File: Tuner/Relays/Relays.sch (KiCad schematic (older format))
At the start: 82 parts, among them J1 Conn_01x03, J10 Conn_01x02, J11 Conn_01x02, J12 Conn_01x01, J13 Conn_01x01, J14 Conn_01x01, J15 Conn_01x01, J16 Conn_01x02, J17 Conn_02x10_Odd_Even, J18 Conn_01x02, J19 Conn_01x03, J2 Conn_01x03, J3 Conn_01x03, J4 Conn_01x03, J5 Conn_01x03, J6 Conn_01x03, J7 Conn_01x03, J8 Conn_01x02, J9 Conn_01x02

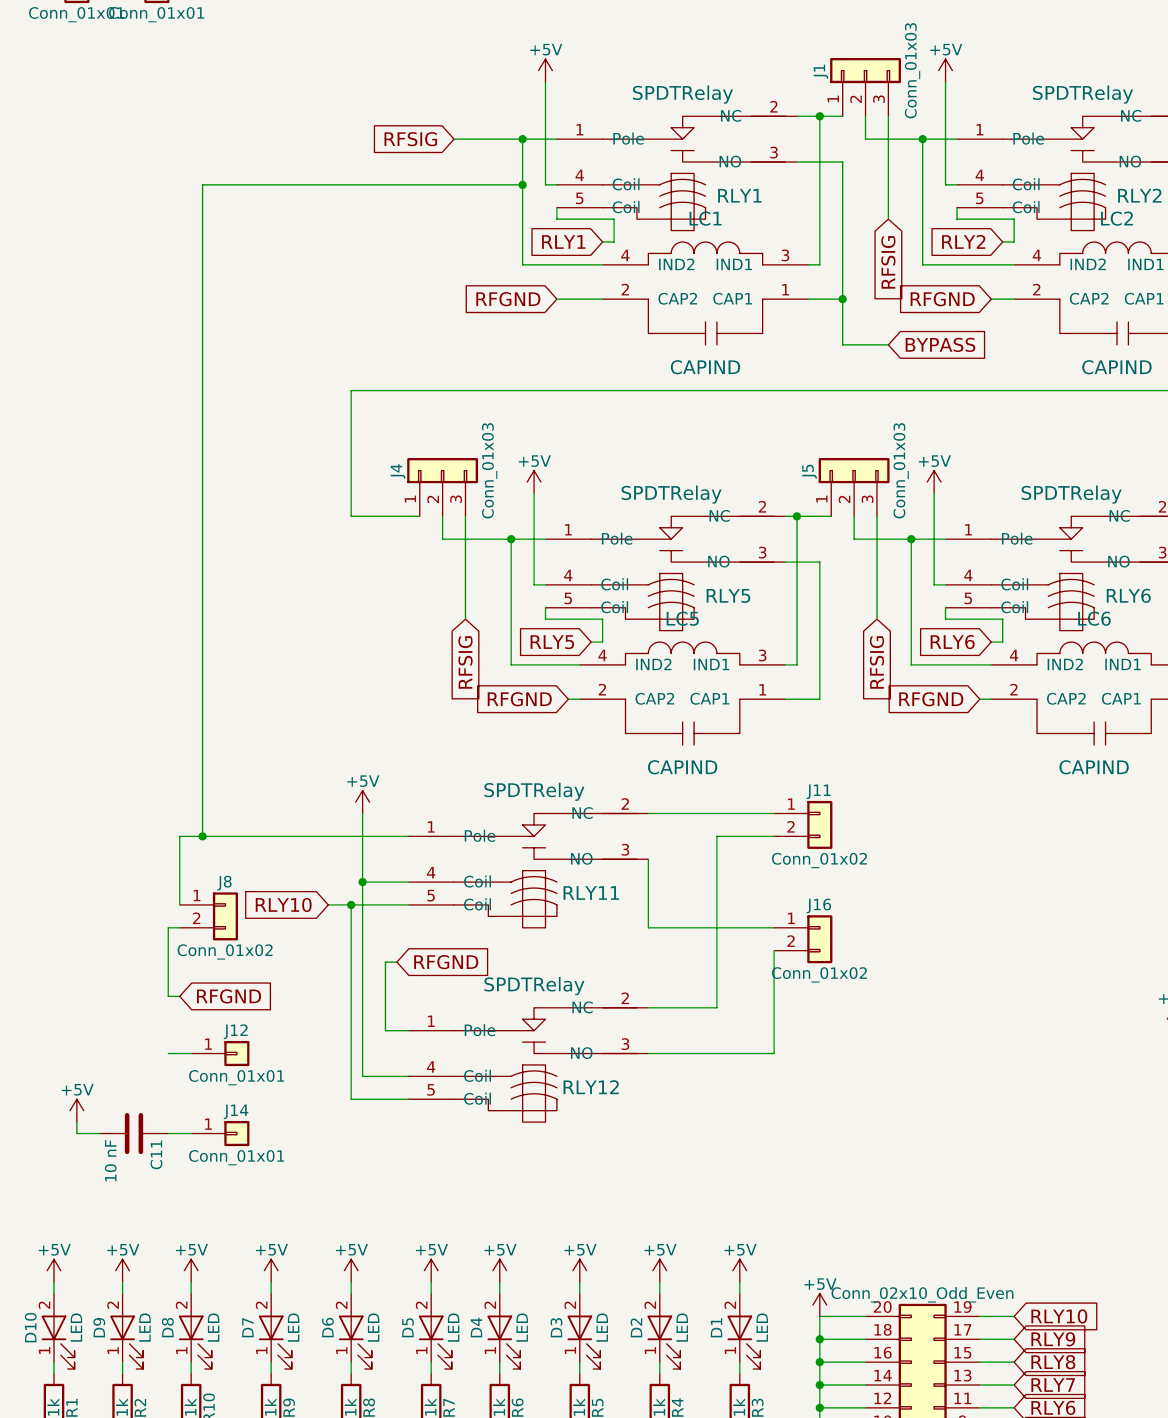
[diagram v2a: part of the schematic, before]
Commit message: Relay boards changed to have coil terminals all on same side
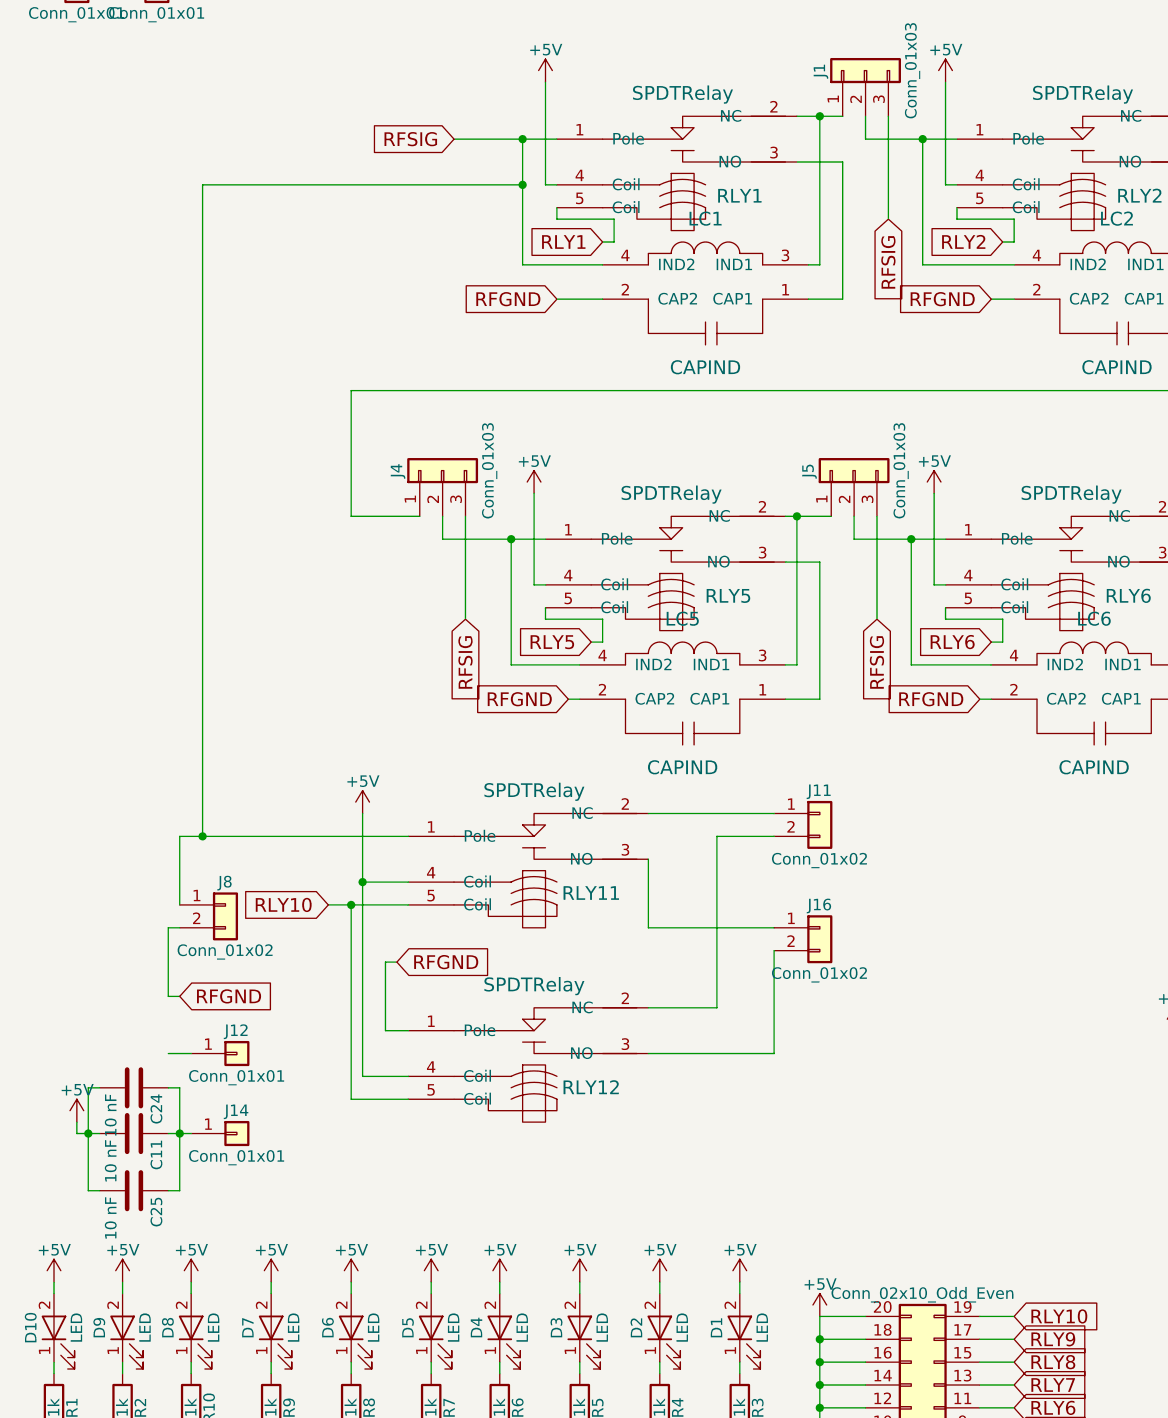
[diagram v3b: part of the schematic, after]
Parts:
- added C24, C25: 10 nF, Capacitors_THT:C_Disc_D5.0mm_W2.5mm_P5.00mm, symbol C
- C11: footprint Capacitors_THT:C_Disc_D5.0mm_W2.5mm_P2.50mm -> Capacitors_THT:C_Disc_D5.0mm_W2.5mm_P5.00mm
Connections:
- net +5V: now also C24.2, C25.2
- net at C11.1, J14.1 (Pin_1): now also C24.1, C25.1
- net BYPASS: no longer names the net of LC1.1 (CAP1), RLY1.3 (NO)

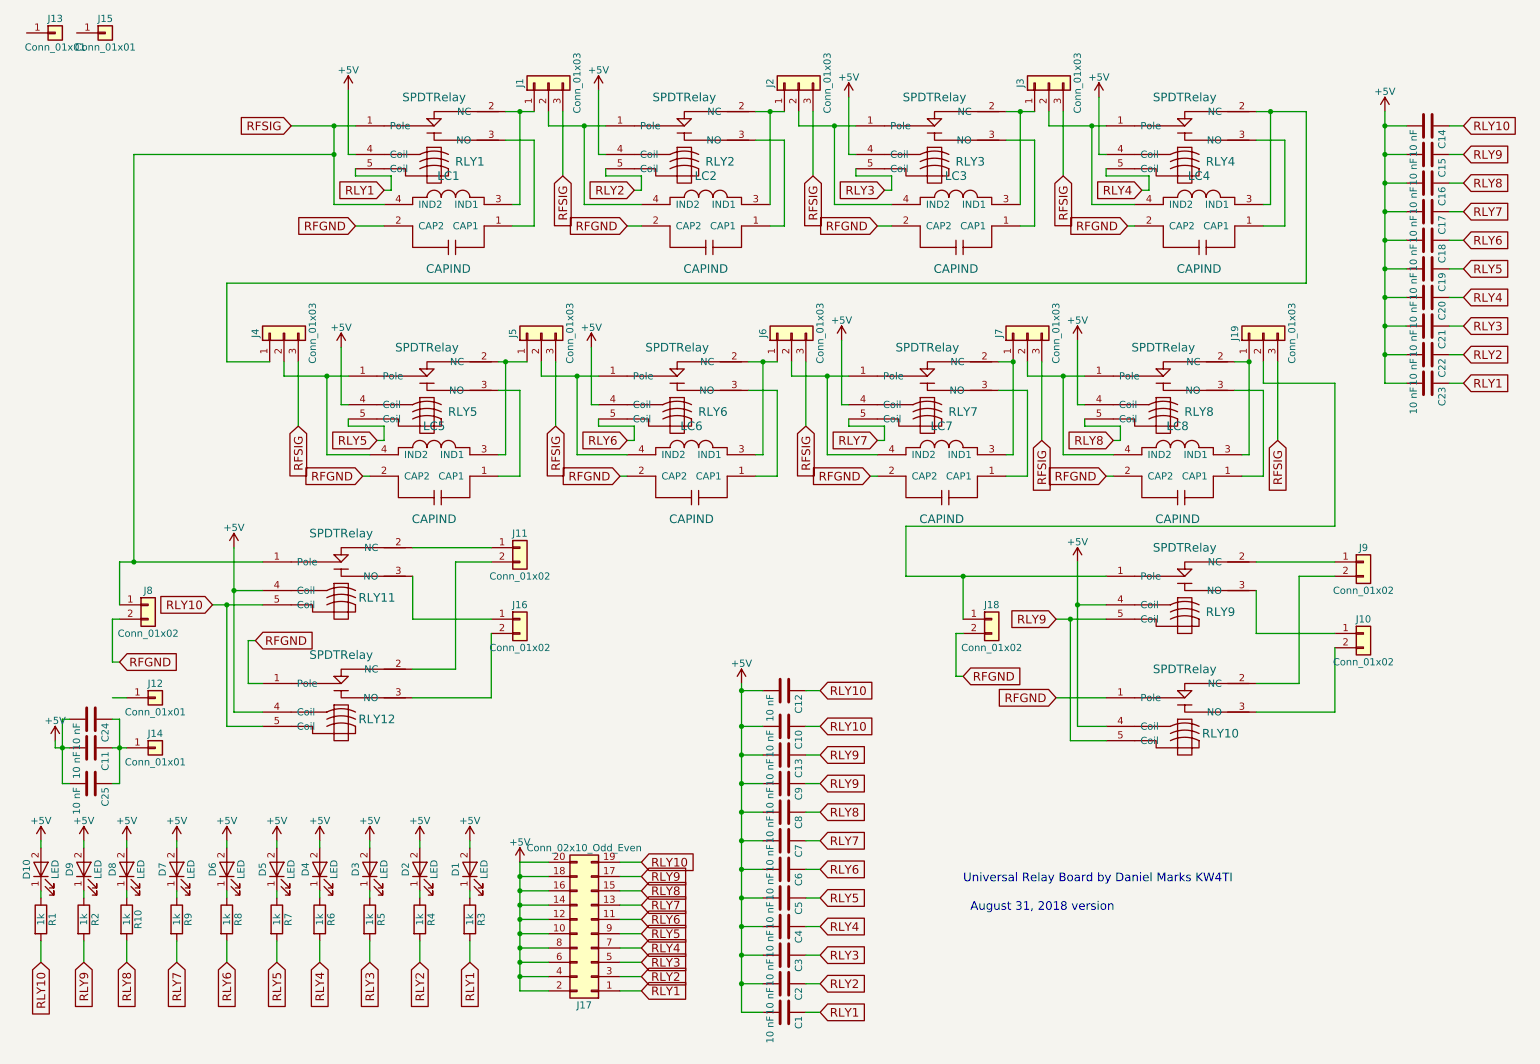
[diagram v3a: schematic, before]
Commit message: Added boards for SMIH/Schrack Relays
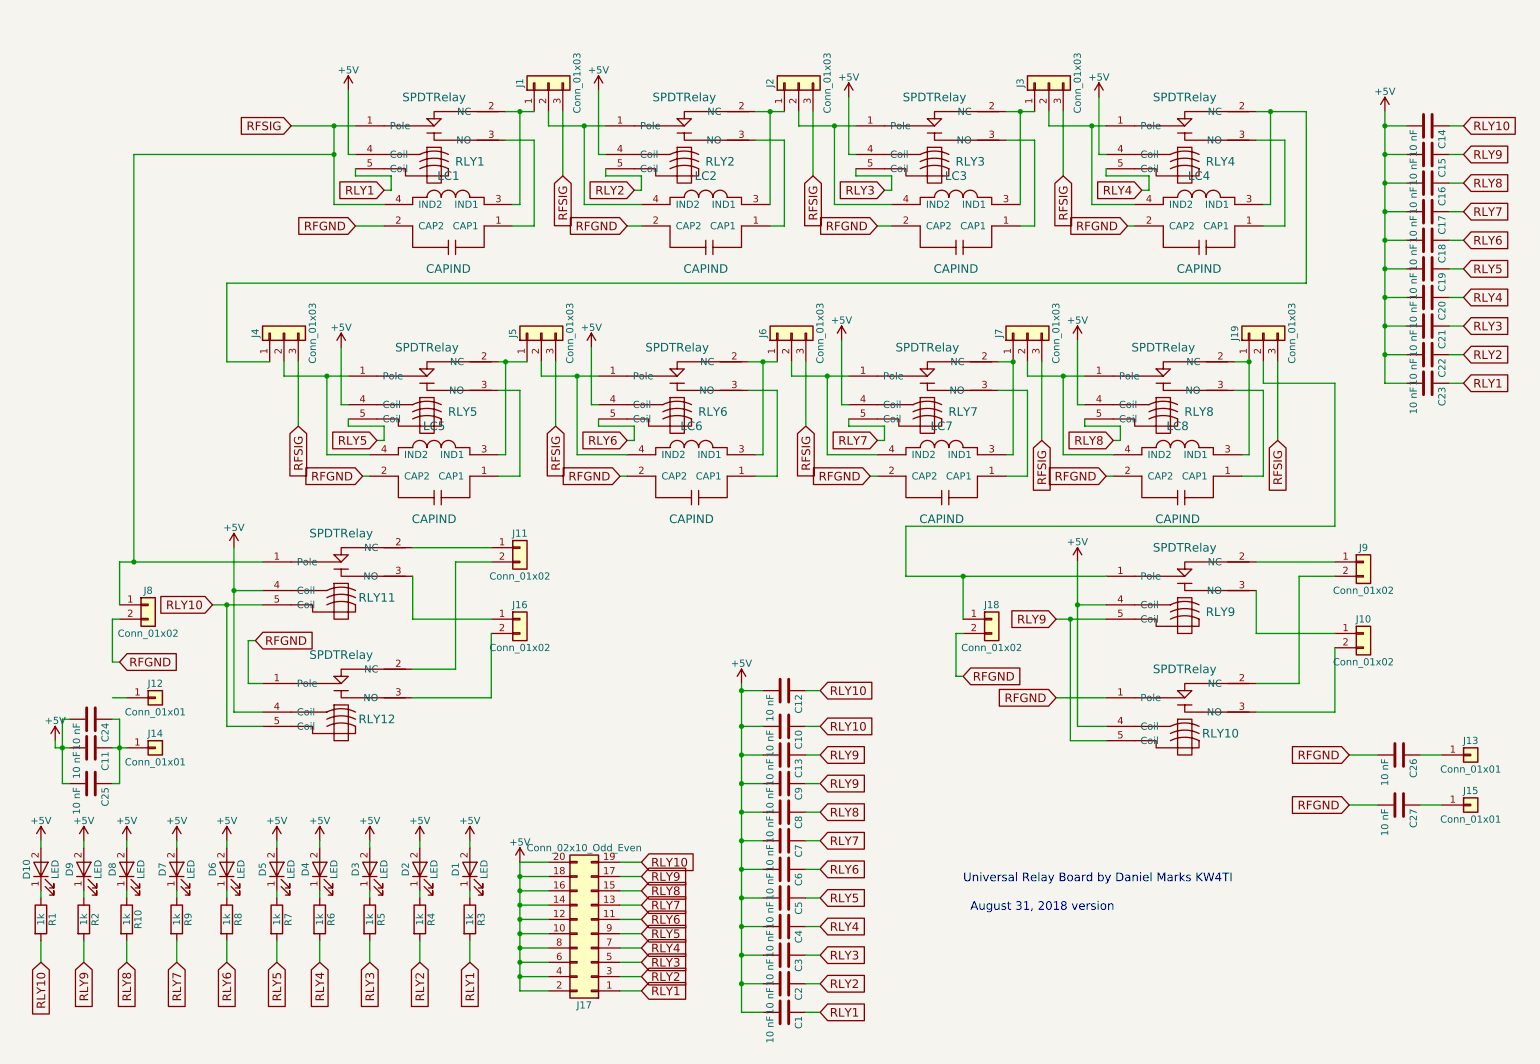
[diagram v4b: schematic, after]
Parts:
- added C26: 10 nF, Capacitors_THT:C_Disc_D5.0mm_W2.5mm_P2.50mm, symbol C
- added C27: 10 nF, Capacitors_THT:C_Disc_D5.0mm_W2.5mm_P5.00mm, symbol C
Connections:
- net RFGND: now also C26.2, C27.2
- net at J13.1 (Pin_1): now also C26.1
- net at J15.1 (Pin_1): now also C27.1
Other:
- moved on the sheet: J13, J15
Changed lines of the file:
@@
 $EndComp
 $Comp
-L +5V #PWR10
+L +5V #PWR01
 U 1 1 5B1A3BAF
 P 2950 2950
-F 0 "#PWR10" H 2950 2800 50  0001 C CNN
+F 0 "#PWR01" H 2950 2800 50  0001 C CNN
 F 1 "+5V" H 2950 3090 50  0000 C CNN
 F 2 "" H 2950 2950 50  0001 C CNN
@@
 $EndComp
 $Comp
-L +5V #PWR16
+L +5V #PWR02
 U 1 1 5B1A3CC8
 P 4700 2950
-F 0 "#PWR16" H 4700 2800 50  0001 C CNN
+F 0 "#PWR02" H 4700 2800 50  0001 C CNN
 F 1 "+5V" H 4700 3090 50  0000 C CNN
 F 2 "" H 4700 2950 50  0001 C CNN
@@
 $EndComp
 $Comp
-L +5V #PWR19
+L +5V #PWR03
 U 1 1 5B1A3D42
 P 6450 2900
-F 0 "#PWR19" H 6450 2750 50  0001 C CNN
+F 0 "#PWR03" H 6450 2750 50  0001 C CNN
 F 1 "+5V" H 6450 3040 50  0000 C CNN
 F 2 "" H 6450 2900 50  0001 C CNN
@@
 $EndComp
 $Comp
-L +5V #PWR22
+L +5V #PWR04
 U 1 1 5B1A3DBC
 P 8100 4450
-F 0 "#PWR22" H 8100 4300 50  0001 C CNN
+F 0 "#PWR04" H 8100 4300 50  0001 C CNN
 F 1 "+5V" H 8100 4590 50  0000 C CNN
 F 2 "" H 8100 4450 50  0001 C CNN
@@
 $EndComp
 $Comp
-L +5V #PWR23
+L +5V #PWR05
 U 1 1 5B1A4C3F
 P 8250 1200
-F 0 "#PWR23" H 8250 1050 50  0001 C CNN
+F 0 "#PWR05" H 8250 1050 50  0001 C CNN
 F 1 "+5V" H 8250 1340 50  0000 C CNN
 F 2 "" H 8250 1200 50  0001 C CNN
@@
 $EndComp
 $Comp
-L +5V #PWR20
+L +5V #PWR06
 U 1 1 5B1A4CB9
 P 6500 1200
-F 0 "#PWR20" H 6500 1050 50  0001 C CNN
+F 0 "#PWR06" H 6500 1050 50  0001 C CNN
 F 1 "+5V" H 6500 1340 50  0000 C CNN
 F 2 "" H 6500 1200 50  0001 C CNN
@@
 $EndComp
 $Comp
-L +5V #PWR17
+L +5V #PWR07
 U 1 1 5B1A4D33
 P 4750 1150
-F 0 "#PWR17" H 4750 1000 50  0001 C CNN
+F 0 "#PWR07" H 4750 1000 50  0001 C CNN
 F 1 "+5V" H 4750 1290 50  0000 C CNN
 F 2 "" H 4750 1150 50  0001 C CNN
@@
 $EndComp
 $Comp
-L +5V #PWR11
+L +5V #PWR08
 U 1 1 5B1A4DAD
 P 3000 1150
-F 0 "#PWR11" H 3000 1000 50  0001 C CNN
+F 0 "#PWR08" H 3000 1000 50  0001 C CNN
 F 1 "+5V" H 3000 1290 50  0000 C CNN
 F 2 "" H 3000 1150 50  0001 C CNN
@@
 L Conn_01x01 J13
 U 1 1 5B19804D
-P 950 750
-F 0 "J13" H 950 850 50  0000 C CNN
-F 1 "Conn_01x01" H 950 650 50  0000 C CNN
-F 2 "Connectors:1pin" H 950 750 50  0001 C CNN
-F 3 "" H 950 750 50  0001 C CNN
-	1    950  750
+P 10850 5800
+F 0 "J13" H 10850 5900 50  0000 C CNN
+F 1 "Conn_01x01" H 10850 5700 50  0000 C CNN
+F 2 "Connectors:1pin" H 10850 5800 50  0001 C CNN
+F 3 "" H 10850 5800 50  0001 C CNN
+	1    10850 5800
 	1    0    0    -1
 $EndComp
@@
 L Conn_01x01 J15
 U 1 1 5B19812D
-P 1300 750
-F 0 "J15" H 1300 850 50  0000 C CNN
-F 1 "Conn_01x01" H 1300 650 50  0000 C CNN
-F 2 "Connectors:1pin" H 1300 750 50  0001 C CNN
-F 3 "" H 1300 750 50  0001 C CNN
-	1    1300 750
+P 10850 6150
+F 0 "J15" H 10850 6250 50  0000 C CNN
+F 1 "Conn_01x01" H 10850 6050 50  0000 C CNN
+F 2 "Connectors:1pin" H 10850 6150 50  0001 C CNN
+F 3 "" H 10850 6150 50  0001 C CNN
+	1    10850 6150
 	1    0    0    -1
 $EndComp
@@
 $EndComp
 $Comp
-L +5V #PWR4
+L +5V #PWR09
 U 1 1 5B25DE9C
 P 1450 6400
-F 0 "#PWR4" H 1450 6250 50  0001 C CNN
+F 0 "#PWR09" H 1450 6250 50  0001 C CNN
 F 1 "+5V" H 1450 6540 50  0000 C CNN
 F 2 "" H 1450 6400 50  0001 C CNN
@@
 $EndComp
 $Comp
-L +5V #PWR5
+L +5V #PWR010
 U 1 1 5B25F712
 P 1800 6400
-F 0 "#PWR5" H 1800 6250 50  0001 C CNN
+F 0 "#PWR010" H 1800 6250 50  0001 C CNN
 F 1 "+5V" H 1800 6540 50  0000 C CNN
 F 2 "" H 1800 6400 50  0001 C CNN
@@
 $EndComp
 $Comp
-L +5V #PWR6
+L +5V #PWR011
 U 1 1 5B25F91B
 P 2150 6400
-F 0 "#PWR6" H 2150 6250 50  0001 C CNN
+F 0 "#PWR011" H 2150 6250 50  0001 C CNN
 F 1 "+5V" H 2150 6540 50  0000 C CNN
 F 2 "" H 2150 6400 50  0001 C CNN
@@
 $EndComp
 $Comp
-L +5V #PWR8
+L +5V #PWR012
 U 1 1 5B25F931
 P 2500 6400
-F 0 "#PWR8" H 2500 6250 50  0001 C CNN
+F 0 "#PWR012" H 2500 6250 50  0001 C CNN
 F 1 "+5V" H 2500 6540 50  0000 C CNN
 F 2 "" H 2500 6400 50  0001 C CNN
@@
 $EndComp
 $Comp
-L +5V #PWR9
+L +5V #PWR013
 U 1 1 5B25FB4D
 P 2800 6400
-F 0 "#PWR9" H 2800 6250 50  0001 C CNN
+F 0 "#PWR013" H 2800 6250 50  0001 C CNN
 F 1 "+5V" H 2800 6540 50  0000 C CNN
 F 2 "" H 2800 6400 50  0001 C CNN
@@
 $EndComp
 $Comp
-L +5V #PWR12
+L +5V #PWR014
 U 1 1 5B25FB63
 P 3150 6400
-F 0 "#PWR12" H 3150 6250 50  0001 C CNN
+F 0 "#PWR014" H 3150 6250 50  0001 C CNN
 F 1 "+5V" H 3150 6540 50  0000 C CNN
 F 2 "" H 3150 6400 50  0001 C CNN
@@
 $EndComp
 $Comp
-L +5V #PWR13
+L +5V #PWR015
 U 1 1 5B25FB79
 P 3500 6400
-F 0 "#PWR13" H 3500 6250 50  0001 C CNN
+F 0 "#PWR015" H 3500 6250 50  0001 C CNN
 F 1 "+5V" H 3500 6540 50  0000 C CNN
 F 2 "" H 3500 6400 50  0001 C CNN
@@
 $EndComp
 $Comp
-L +5V #PWR14
+L +5V #PWR016
 U 1 1 5B25FB8F
 P 3850 6400
-F 0 "#PWR14" H 3850 6250 50  0001 C CNN
+F 0 "#PWR016" H 3850 6250 50  0001 C CNN
 F 1 "+5V" H 3850 6540 50  0000 C CNN
 F 2 "" H 3850 6400 50  0001 C CNN
@@
 RLY10
 $Comp
-L +5V #PWR15
+L +5V #PWR017
 U 1 1 5B89A678
 P 4200 6550
-F 0 "#PWR15" H 4200 6400 50  0001 C CNN
+F 0 "#PWR017" H 4200 6400 50  0001 C CNN
 F 1 "+5V" H 4200 6690 50  0000 C CNN
 F 2 "" H 4200 6550 50  0001 C CNN
@@
 $EndComp
 $Comp
-L +5V #PWR3
+L +5V #PWR018
 U 1 1 5B89BB19
 P 1150 6400
-F 0 "#PWR3" H 1150 6250 50  0001 C CNN
+F 0 "#PWR018" H 1150 6250 50  0001 C CNN
 F 1 "+5V" H 1150 6540 50  0000 C CNN
 F 2 "" H 1150 6400 50  0001 C CNN
@@
 $EndComp
 $Comp
-L +5V #PWR1
+L +5V #PWR019
 U 1 1 5B89BBCB
 P 850 6400
-F 0 "#PWR1" H 850 6250 50  0001 C CNN
+F 0 "#PWR019" H 850 6250 50  0001 C CNN
 F 1 "+5V" H 850 6540 50  0000 C CNN
 F 2 "" H 850 6400 50  0001 C CNN
@@
 RLY9
 $Comp
-L +5V #PWR18
+L +5V #PWR020
 U 1 1 5B89FB34
 P 5750 5300
-F 0 "#PWR18" H 5750 5150 50  0001 C CNN
+F 0 "#PWR020" H 5750 5150 50  0001 C CNN
 F 1 "+5V" H 5750 5440 50  0000 C CNN
 F 2 "" H 5750 5300 50  0001 C CNN
@@
 RLY8
 $Comp
-L +5V #PWR21
+L +5V #PWR021
 U 1 1 5B8A1B7B
 P 8100 2900
-F 0 "#PWR21" H 8100 2750 50  0001 C CNN
+F 0 "#PWR021" H 8100 2750 50  0001 C CNN
 F 1 "+5V" H 8100 3040 50  0000 C CNN
 F 2 "" H 8100 2900 50  0001 C CNN
@@
 $EndComp
 $Comp
-L +5V #PWR7
+L +5V #PWR022
 U 1 1 5B8A2542
 P 2200 4350
-F 0 "#PWR7" H 2200 4200 50  0001 C CNN
+F 0 "#PWR022" H 2200 4200 50  0001 C CNN
 F 1 "+5V" H 2200 4490 50  0000 C CNN
 F 2 "" H 2200 4350 50  0001 C CNN
@@
 $EndComp
 $Comp
-L +5V #PWR2
+L +5V #PWR023
 U 1 1 5B97C780
 P 950 5700
-F 0 "#PWR2" H 950 5550 50  0001 C CNN
+F 0 "#PWR023" H 950 5550 50  0001 C CNN
 F 1 "+5V" H 950 5840 50  0000 C CNN
 F 2 "" H 950 5700 50  0001 C CNN
@@
 RLY9
 $Comp
-L +5V #PWR24
+L +5V #PWR024
 U 1 1 5BA3849B
 P 10250 1300
-F 0 "#PWR24" H 10250 1150 50  0001 C CNN
+F 0 "#PWR024" H 10250 1150 50  0001 C CNN
 F 1 "+5V" H 10250 1440 50  0000 C CNN
 F 2 "" H 10250 1300 50  0001 C CNN
@@
 Wire Wire Line
 	1000 6000 1050 6000
+$Comp
+L C C26
+U 1 1 5BCBEB36
+P 10350 5800
+F 0 "C26" H 10375 5900 50  0000 L CNN
+F 1 "10 nF" H 10375 5700 50  0000 L CNN
+F 2 "Capacitors_THT:C_Disc_D5.0mm_W2.5mm_P2.50mm" H 10388 5650 50  0001 C CNN
+F 3 "" H 10350 5800 50  0001 C CNN
+	1    10350 5800
+	0    1    1    0
+$EndComp
+Text GLabel 10000 5800 0    60   Input ~ 0
+RFGND
+Wire Wire Line
+	10000 5800 10200 5800
+Text GLabel 10000 6150 0    60   Input ~ 0
+RFGND
+$Comp
+L C C27
+U 1 1 5BCBF354
+P 10350 6150
+F 0 "C27" H 10375 6250 50  0000 L CNN
+F 1 "10 nF" H 10375 6050 50  0000 L CNN
+F 2 "Capacitors_THT:C_Disc_D5.0mm_W2.5mm_P5.00mm" H 10388 6000 50  0001 C CNN
+F 3 "" H 10350 6150 50  0001 C CNN
+	1    10350 6150
+	0    1    1    0
+$EndComp
+Wire Wire Line
+	10200 6150 10000 6150
+Wire Wire Line
+	10650 6150 10500 6150
+Wire Wire Line
+	10650 5800 10500 5800
 $EndSCHEMATC
